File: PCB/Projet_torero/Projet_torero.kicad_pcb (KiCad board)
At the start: 2 copper layers, 54 x 57 mm, 73 parts, among them IC501 MP1475SGJ-P, J201 Conn_02x07_Odd_Even, J202 Conn_02x08_Odd_Even, J401 Conn_01x08, J501 Conn_01x02, J601 Conn_01x06, J701 Conn_01x06, SW201 SW_Push, SW202 SW_Push, U201 STM32G431CBUx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

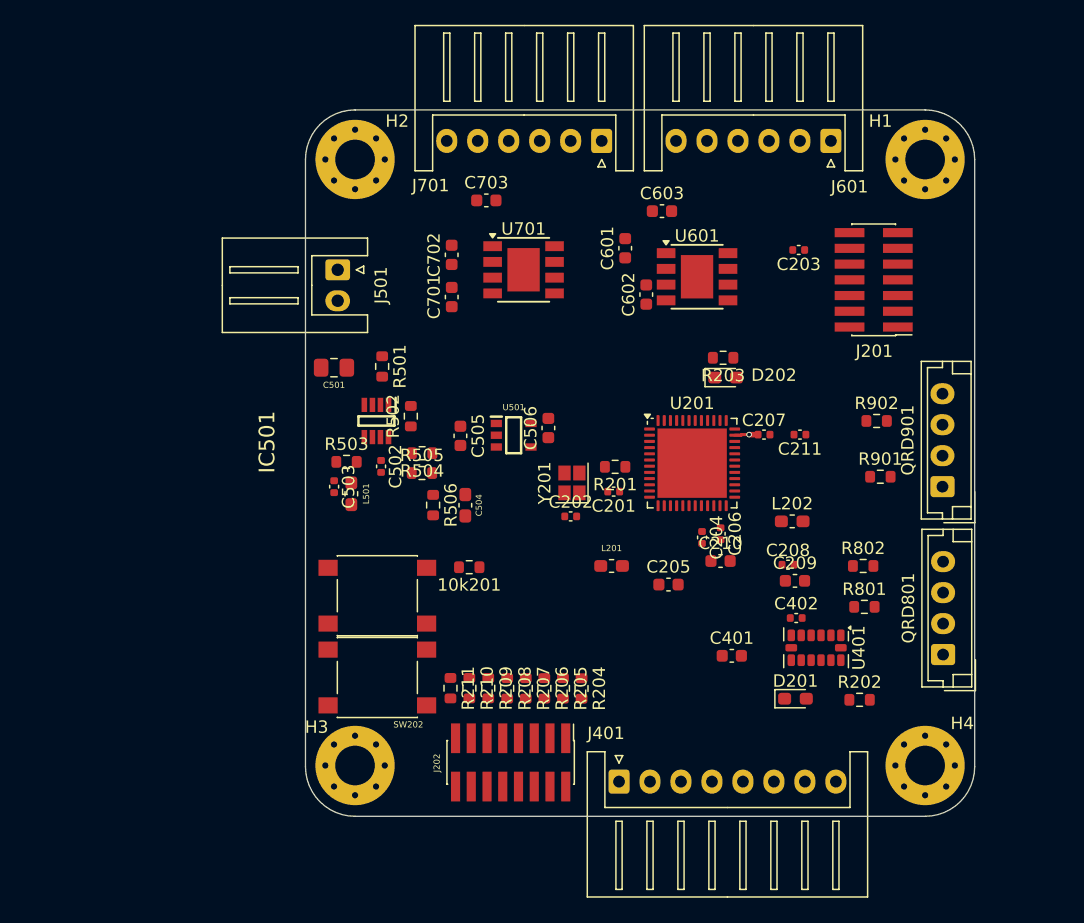
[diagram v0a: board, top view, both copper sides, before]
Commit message: modif placement composant
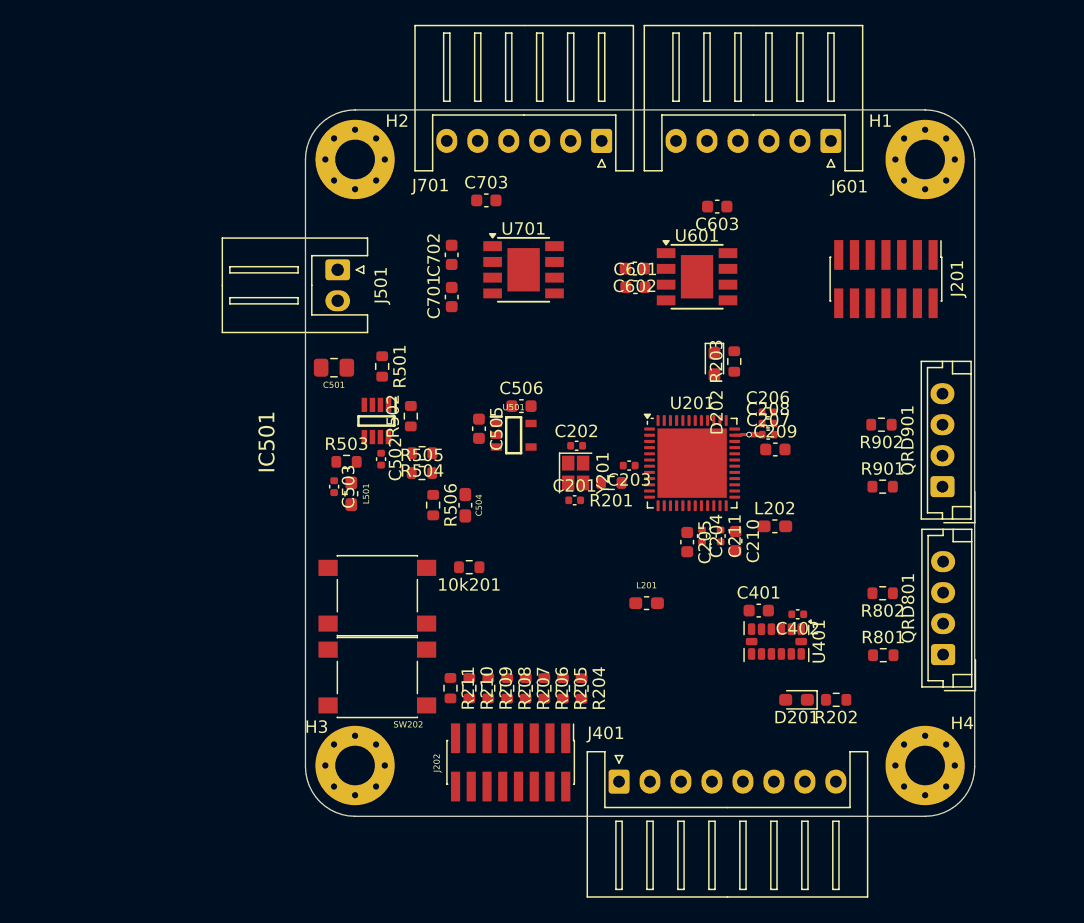
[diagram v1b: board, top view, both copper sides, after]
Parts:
- moved C203 22.1 mm to (166.1, 78.7)
- moved C208 11.5 mm to (177.3, 75.3)
- moved C209 10.7 mm to (177.9, 77.4)
- moved C206 10.5 mm to (177.3, 74.4), turned to 0 degrees
- moved C211 10.4 mm to (173.5, 84.4), turned to -90 degrees
- moved C202 5.72 mm to (161.9, 77.1)
- moved C603 4.47 mm to (173.2, 57.8), turned to 180 degrees
- moved C401 4.25 mm to (176.6, 90.4)
- moved R801 4.19 mm to (186.6, 94.0)
- moved L201 4.12 mm to (167.5, 89.8)
- moved C205 3.74 mm to (170.8, 84.9), turned to -90 degrees
- moved C601 3.25 mm to (166.6, 64.3), turned to 0 degrees
- moved U401 3.24 mm to (178.0, 92.9)
- moved C201 3.22 mm to (161.7, 81.5), turned to 0 degrees
- moved C506 2.80 mm to (157.4, 73.9), turned to 0 degrees
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
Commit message: modif routing
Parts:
- removed L201: L, Inductor_SMD:L_0603_1608Metric_Pad1.05x0.95mm_HandSolder

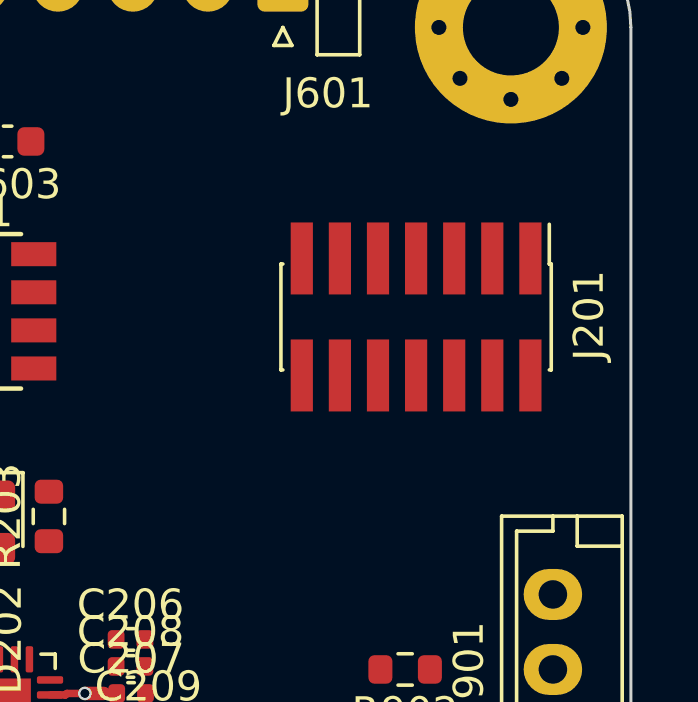
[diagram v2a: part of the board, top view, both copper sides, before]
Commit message: Ajout Switch ON/OFF sur carte
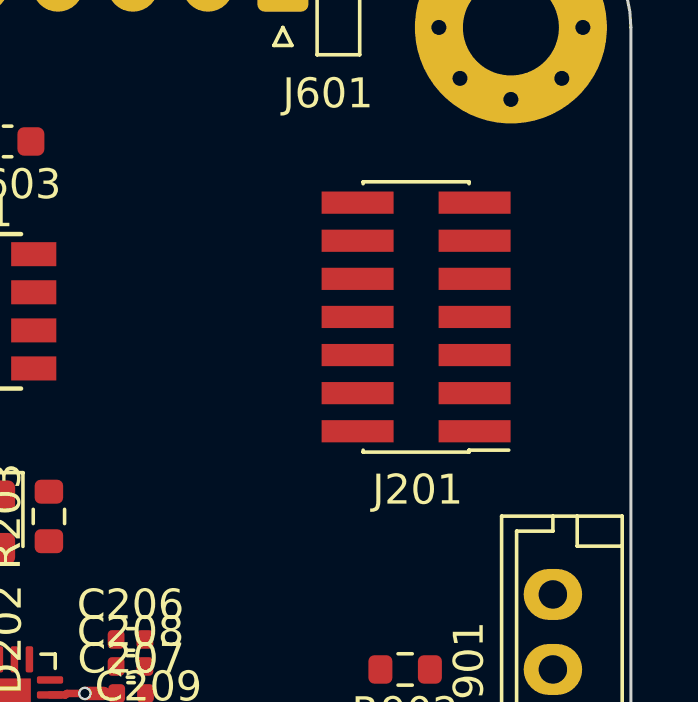
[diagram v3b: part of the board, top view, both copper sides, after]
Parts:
- turned J201 to 180 degrees

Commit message: Nouvelle version avec Empreinte correcte
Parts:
- added J502: Conn_01x03, Connector_JST:JST_XH_S3B-XH-A_1x03_P2.50mm_Horizontal, F.Cu at (127.7, 69.7)
- L202: footprint Inductor_SMD:L_0603_1608Metric_Pad1.05x0.95mm_HandSolder -> Inductor_SMD:L_Wuerth_WE-TPC-3816
- moved SW201 23.8 mm to (122.1, 91.6)
- moved SW202 23.8 mm to (122.1, 98.2)
- moved C602 5.23 mm to (171.8, 62.3)
- moved C603 5.23 mm to (178.4, 57.3)
- moved U601 5.23 mm to (176.8, 62.9)
- moved U701 5.23 mm to (162.8, 62.4)
- moved C601 5.23 mm to (171.8, 63.8)
- moved C702 5.23 mm to (157.0, 61.2)
- moved C703 5.23 mm to (159.8, 56.8)
- moved C701 5.23 mm to (157.0, 64.6)
- moved C505 4.24 mm to (155.4, 71.7)
- moved C506 4.24 mm to (158.8, 69.9)
- moved U501 4.24 mm to (158.2, 72.2)
- moved C501 3.50 mm to (145.8, 70.8)
- moved R501 3.50 mm to (149.7, 70.7)
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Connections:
- C204 pad 1: +3.3V -> Net-(U201-VBAT)
- C205 pad 1: +3.3V -> Net-(U201-VBAT)
- C210 pad 1: +3.3V -> Net-(U201-VBAT)
- C211 pad 1: +3.3V -> Net-(U201-VBAT)
- C402 pad 1: +3.3V -> GND
- C402 pad 2: GND -> +3.3V
- J202 pad 1: Net-(J202-Pin_1) -> GND
- J202 pad 10: GND -> Net-(J202-Pin_10)
- J202 pad 11: Net-(J202-Pin_11) -> GND
- J202 pad 12: GND -> Net-(J202-Pin_12)
- J202 pad 13: Net-(J202-Pin_13) -> GND
- J202 pad 14: GND -> Net-(J202-Pin_14)
- J202 pad 15: Net-(J202-Pin_15) -> GND
- J202 pad 16: GND -> Net-(J202-Pin_16)
- J202 pad 2: GND -> Net-(J202-Pin_2)
- J202 pad 3: Net-(J202-Pin_3) -> GND
- J202 pad 4: GND -> Net-(J202-Pin_4)
- J202 pad 5: Net-(J202-Pin_5) -> GND
- J202 pad 6: GND -> Net-(J202-Pin_6)
- J202 pad 7: Net-(J202-Pin_7) -> GND
- J202 pad 8: GND -> Net-(J202-Pin_8)
- J202 pad 9: Net-(J202-Pin_9) -> GND
- J501 pad 2: 7.2V -> Net-(J501-Pin_2)
- L202 pad 2: +3.3V -> Net-(U201-VBAT)
- R204 pad 2: Net-(J202-Pin_1) -> Net-(J202-Pin_2)
- R205 pad 2: Net-(J202-Pin_3) -> Net-(J202-Pin_4)
- R206 pad 2: Net-(J202-Pin_5) -> Net-(J202-Pin_6)
- R207 pad 2: Net-(J202-Pin_7) -> Net-(J202-Pin_8)
- R208 pad 2: Net-(J202-Pin_9) -> Net-(J202-Pin_10)
- R209 pad 2: Net-(J202-Pin_11) -> Net-(J202-Pin_12)
- R210 pad 2: Net-(J202-Pin_13) -> Net-(J202-Pin_14)
- R211 pad 2: Net-(J202-Pin_15) -> Net-(J202-Pin_16)
- U201 pad 1: +3.3V -> Net-(U201-VBAT)
- U201 pad 20: +3.3V -> Net-(U201-VBAT)
- U201 pad 21: +3.3V -> Net-(U201-VBAT)
- U201 pad 26: /STM32/SPI2_SCK -> /CAPTEURS/SCLK_ACC

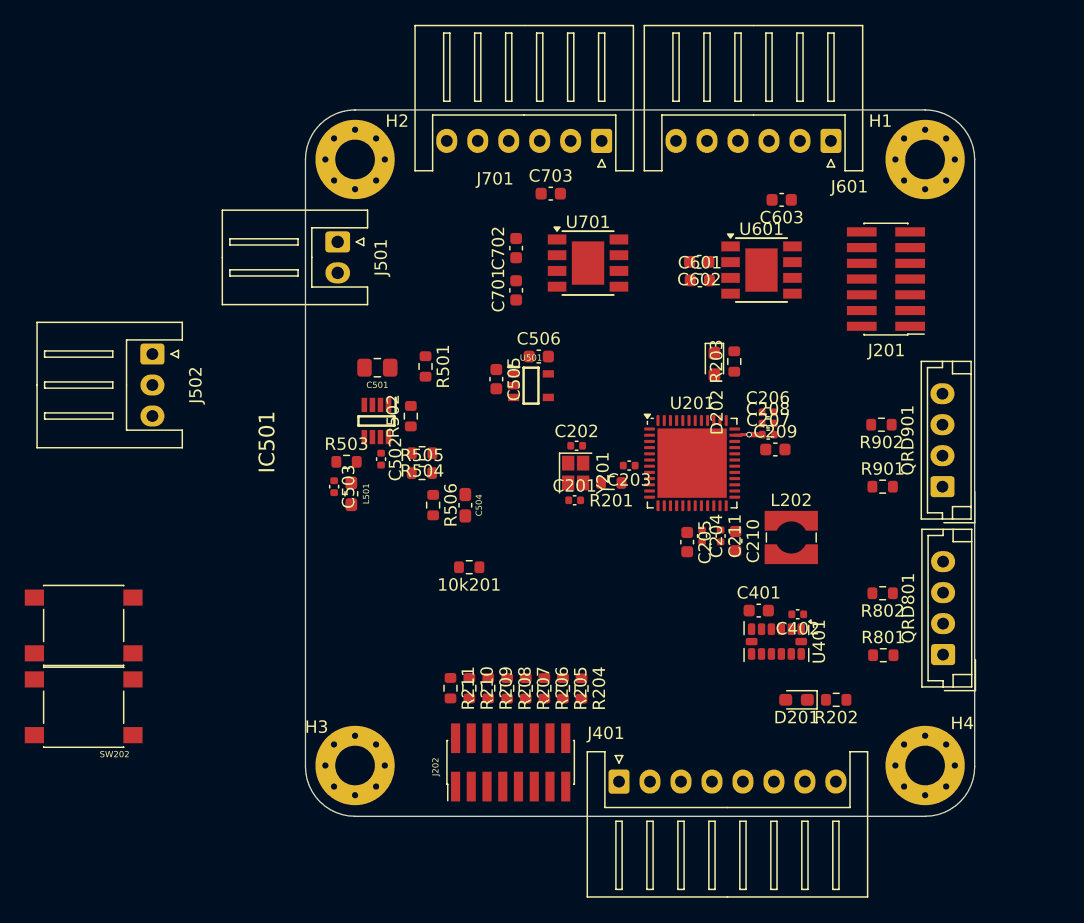
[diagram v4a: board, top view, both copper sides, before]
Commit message: Placement des composants
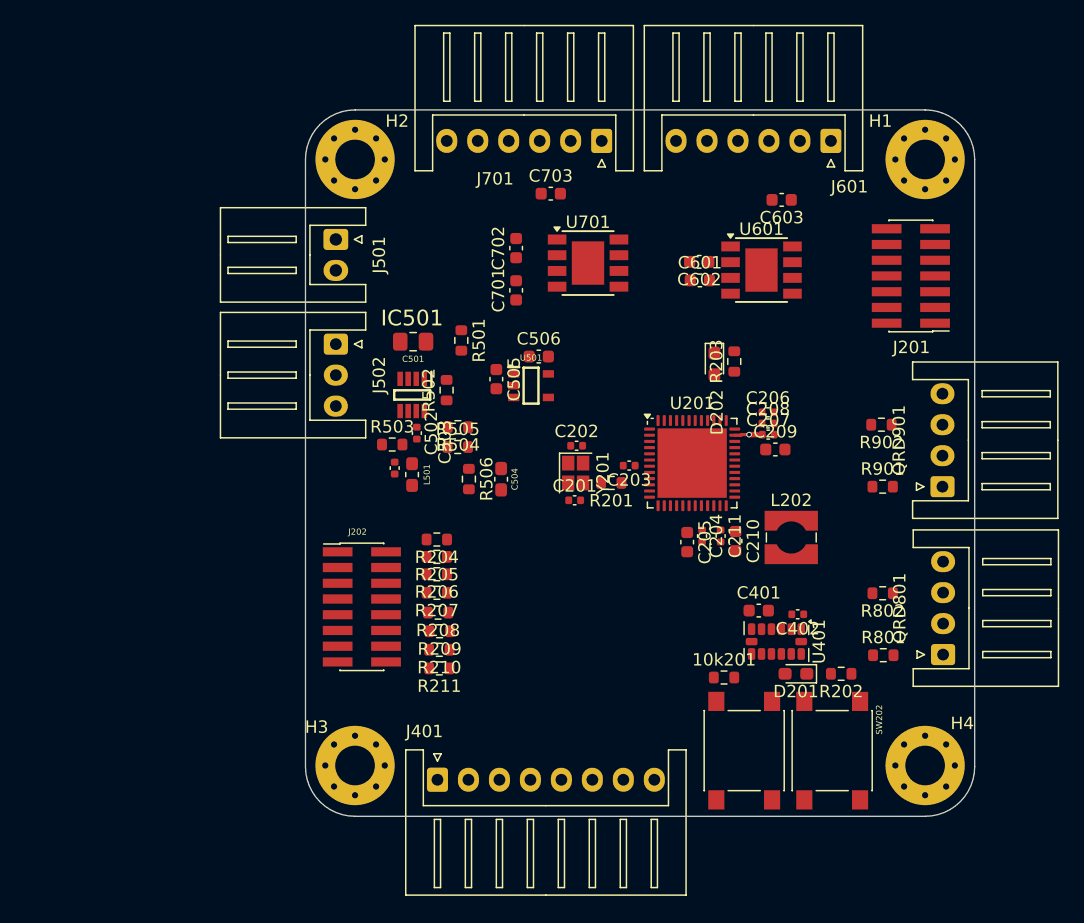
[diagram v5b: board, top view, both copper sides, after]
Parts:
- QRD801, QRD901: footprint Connector_JST:JST_EH_B4B-EH-A_1x04_P2.50mm_Vertical -> Connector_JST:JST_XH_S4B-XH-A_1x04_P2.50mm_Horizontal
- moved SW202 60.5 mm to (182.5, 101.7), turned to -90 degrees
- moved SW201 54.2 mm to (175.4, 101.7), turned to 90 degrees
- moved 10k201 22.4 mm to (173.8, 95.8), turned to 0 degrees
- moved J202 17.4 mm to (144.6, 90.1), turned to 0 degrees
- moved R204 16.8 mm to (150.6, 84.7), turned to 180 degrees
- moved J502 14.8 mm to (142.4, 68.9)
- moved R205 14.7 mm to (150.6, 86.1), turned to 180 degrees
- moved J401 14.7 mm to (150.7, 104.0)
- moved R206 12.7 mm to (150.6, 87.5), turned to 180 degrees
- moved R207 10.5 mm to (150.6, 89.0), turned to 180 degrees
- moved R208 8.27 mm to (150.7, 90.6), turned to 180 degrees
- moved R209 6.05 mm to (150.8, 92.1), turned to 180 degrees
- moved L501 5.14 mm to (148.6, 79.4)
- moved C503 5.11 mm to (147.2, 78.9)
- moved R503 3.94 mm to (147.0, 77.0)
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
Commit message: Placement des composant "terminé"
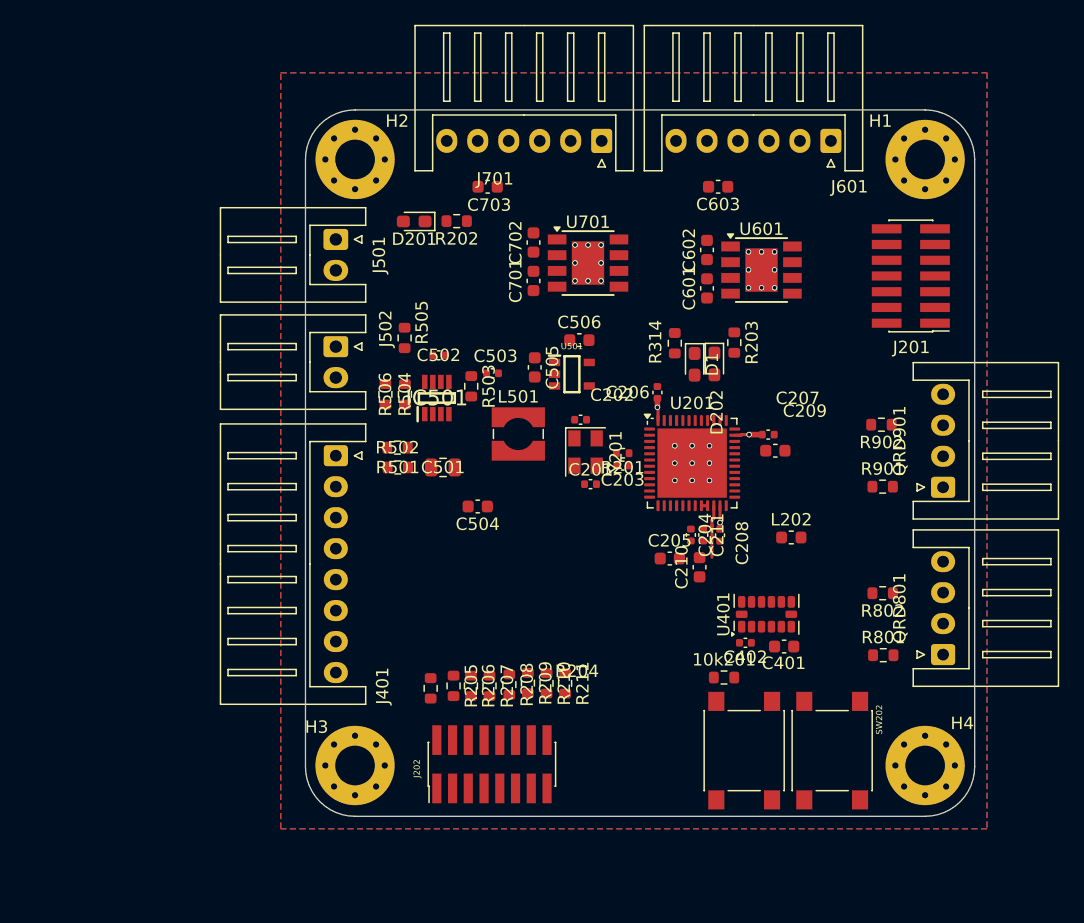
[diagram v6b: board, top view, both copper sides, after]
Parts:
- added D1: Red, LED_SMD:LED_0603_1608Metric_Pad1.05x0.95mm_HandSolder, F.Cu at (171.4, 70.5)
- added R314: 140, Resistor_SMD:R_0603_1608Metric, F.Cu at (169.8, 68.8)
- C501: footprint Capacitor_SMD:C_0805_2012Metric_Pad1.18x1.45mm_HandSolder -> Capacitor_SMD:C_0805_2012Metric
- C504: footprint Capacitor_SMD:C_0603_1608Metric_Pad1.08x0.95mm_HandSolder -> Capacitor_SMD:C_0603_1608Metric
- J502: value Conn_01x03 -> Conn_01x02; footprint Connector_JST:JST_XH_S3B-XH-A_1x03_P2.50mm_Horizontal -> Connector_JST:JST_XH_S2B-XH-A_1x02_P2.50mm_Horizontal
- L202: footprint Inductor_SMD:L_Wuerth_WE-TPC-3816 -> Inductor_SMD:L_0603_1608Metric
- L501: footprint Inductor_SMD:L_0603_1608Metric_Pad1.05x0.95mm_HandSolder -> Inductor_SMD:L_Wuerth_WE-TPC-3816
- R201: footprint Resistor_SMD:R_0603_1608Metric -> Resistor_SMD:R_0402_1005Metric
- Y201: footprint Crystal:Crystal_SMD_EuroQuartz_X22-4Pin_2.5x2.0mm -> Crystal:Crystal_SMD_EuroQuartz_MT-4Pin_3.2x2.5mm
- moved R202 47.9 mm to (152.2, 59.0)
- moved D201 47.8 mm to (148.8, 59.0)
- moved J401 27.4 mm to (142.4, 77.9), turned to -90 degrees
- moved J202 16.5 mm to (155.0, 102.8), turned to 90 degrees
- moved R204 12.0 mm to (150.1, 96.7), turned to -90 degrees
- moved R501 11.5 mm to (147.4, 78.8), turned to 180 degrees
- moved C503 11.0 mm to (155.1, 71.2), turned to 0 degrees
- moved R205 10.5 mm to (151.9, 96.5), turned to -90 degrees
- moved C501 10.4 mm to (151.1, 78.8), turned to 0 degrees
- moved R211 10.2 mm to (160.9, 96.3), turned to -90 degrees
- moved C208 9.82 mm to (173.4, 84.3), turned to -90 degrees
- moved R505 9.79 mm to (148.0, 68.4), turned to -90 degrees
- moved R506 9.60 mm to (146.4, 73.0)
- moved R206 9.42 mm to (153.3, 96.5), turned to -90 degrees
- moved L501 9.18 mm to (157.2, 76.2), turned to 0 degrees
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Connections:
- net Net-(U201-PB8) renamed /STM32/USER_BTN
- C601 pad 2: V7.2 -> 7.2V
- C602 pad 1: V7.2 -> 7.2V
- C701 pad 2: V7.2 -> 7.2V
- C702 pad 1: V7.2 -> 7.2V
- J502 pad 2: GND -> 7.2V
- U201 pad 40: unconnected-(U201-PC11-Pad40) -> STATUS_LED_Debug
- U601 pad 2: V7.2 -> 7.2V
- U601 pad 3: V7.2 -> 7.2V
- U601 pad 6: V7.2 -> 7.2V
- U701 pad 2: V7.2 -> 7.2V
- U701 pad 3: V7.2 -> 7.2V
- U701 pad 6: V7.2 -> 7.2V
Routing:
- net /CAPTEURS/Rx_LIDAR: track 0.00 -> 4.31 mm
- net +3.3V: track 1.89 -> 6.02 mm, vias 1 -> 3
- net Net-(U201-VBAT): track 0.00 -> 0.50 mm
- net GND: vias 0 -> 25
- added copper zone on In2.Cu, net +3.3V
- added copper zone on In2.Cu, net 7.2V
- added copper zone on B.Cu, net GND
- added copper zone on F.Cu, net GND
- added copper zone on In1.Cu, net GND
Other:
- copper layers 2 -> 4
